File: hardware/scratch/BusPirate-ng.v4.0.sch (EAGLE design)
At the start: 131 parts, among them CON1 CON-USB-F-MICRO-B, IC1 IC_UC_STM32F103RBTXX-LQFP64, IC10 74LVC1G07DBV, IC11 IC_BUFF_SN74LVC1T45DBV, IC12 74LVC1G07DBV, IC13 IC_BUFF_SN74LVC1T45DBV, IC14 74LVC1G07DBV, IC15 IC_BUFF_SN74LVC1T45DBV, IC16 74LVC1G07DBV, IC17 IC_BUFF_SN74LVC1T45DBV, IC2 IC_MEM_23LC1024, IC3 IC_MEM_23LC1024, IC4 IC_74AC573, IC5 IC_BL1551, IC6 IC_BL1551, IC7 74HCT4066PW, IC8 74LVC1G07DBV, IC9 IC_BUFF_SN74LVC1T45DBV, J1 CON_HEADER_1X04, J2 CON_HEADER_1X03-PTH, J3 CON_HEADER_2X02-PTH, J4 CON_HEADER_1X10-RIGHT_ANGLED_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, U1 IC_FPGA_ICE40HX4K, U2 IC_UC_STM32F103ZX, U3 IC_MEM_AT45DB041D

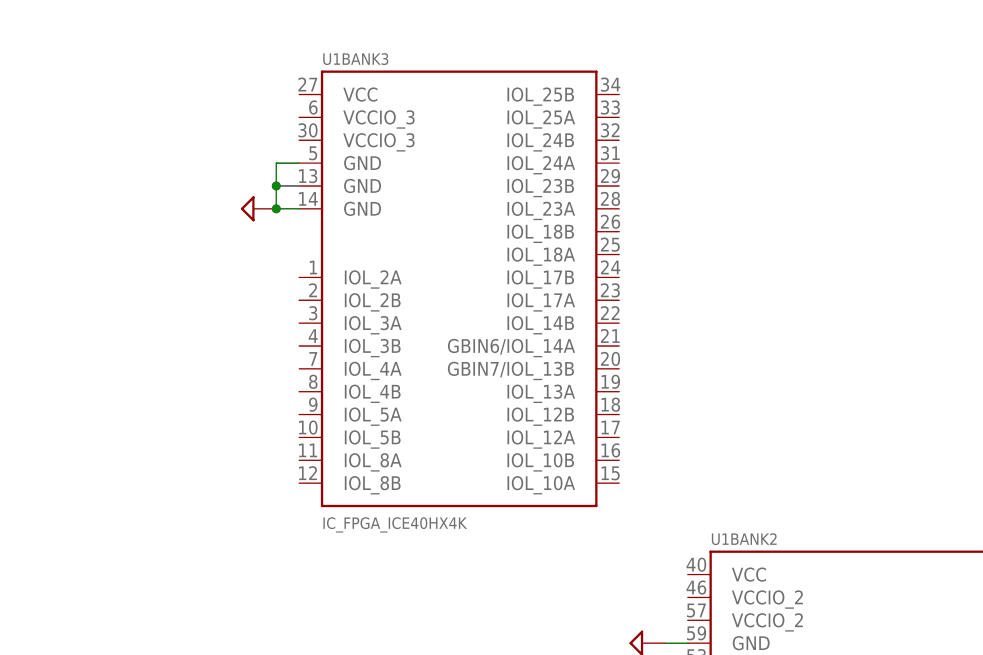
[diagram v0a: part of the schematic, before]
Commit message: connect ARM chip's FSMC address, data and control pins except CS to FPGA
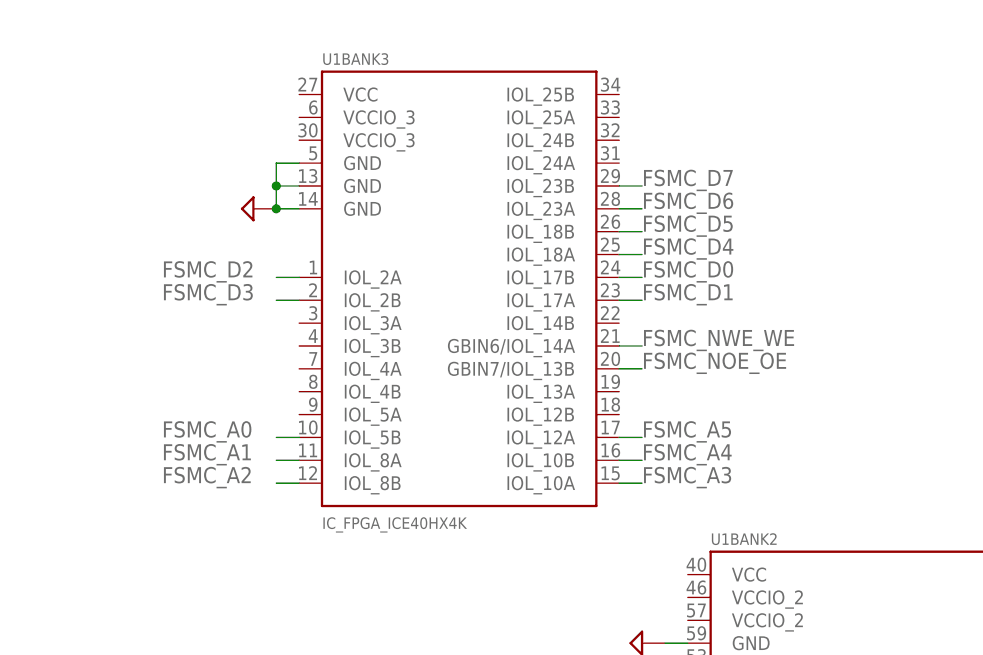
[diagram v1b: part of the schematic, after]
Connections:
- net FSMC_A0: now also U1BANK3.IOL_5B
- net FSMC_A1: now also U1BANK3.IOL_8A
- net FSMC_A2: now also U1BANK3.IOL_8B
- net FSMC_A3: now also U1BANK3.IOL_10A
- net FSMC_A4: now also U1BANK3.IOL_10B
- net FSMC_A5: now also U1BANK3.IOL_12A
- net FSMC_D0: now also U1BANK3.IOL_17B
- net FSMC_D1: now also U1BANK3.IOL_17A
- net FSMC_D2: now also U1BANK3.IOL_2A
- net FSMC_D3: now also U1BANK3.IOL_2B
- net FSMC_D4: now also U1BANK3.IOL_18A
- net FSMC_D5: now also U1BANK3.IOL_18B
- net FSMC_D6: now also U1BANK3.IOL_23A
- net FSMC_D7: now also U1BANK3.IOL_23B
- net FSMC_NOE_OE: now also U1BANK3.GBIN7/IOL_13B
- net FSMC_NWE_WE: now also U1BANK3.GBIN6/IOL_14A
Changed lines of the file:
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@@
 <label x="-241.3" y="426.72" size="1.778" layer="95"/>
+</segment>
+<segment>
+<pinref part="U1" gate="BANK3" pin="IOL_2A"/>
+<wire x1="-38.1" y1="396.24" x2="-40.64" y2="396.24" width="0.1524" layer="91"/>
+<label x="-53.34" y="396.24" size="1.778" layer="95"/>
 </segment>
 </net>
@@
 <label x="-241.3" y="424.18" size="1.778" layer="95"/>
 </segment>
+<segment>
+<pinref part="U1" gate="BANK3" pin="IOL_2B"/>
+<wire x1="-38.1" y1="393.7" x2="-40.64" y2="393.7" width="0.1524" layer="91"/>
+<label x="-53.34" y="393.7" size="1.778" layer="95"/>
+</segment>
 </net>
 <net name="FSMC_NOE_OE" class="0">
@@
 <wire x1="-215.9" y1="416.56" x2="-228.6" y2="416.56" width="0.1524" layer="91"/>
 <label x="-241.3" y="416.56" size="1.778" layer="95"/>
+</segment>
+<segment>
+<pinref part="U1" gate="BANK3" pin="GBIN7/IOL_13B"/>
+<wire x1="-2.54" y1="386.08" x2="0" y2="386.08" width="0.1524" layer="91"/>
+<label x="0" y="386.08" size="1.778" layer="95"/>
 </segment>
 </net>
@@
 <label x="-241.3" y="414.02" size="1.778" layer="95"/>
 </segment>
+<segment>
+<pinref part="U1" gate="BANK3" pin="GBIN6/IOL_14A"/>
+<wire x1="-2.54" y1="388.62" x2="0" y2="388.62" width="0.1524" layer="91"/>
+<label x="0" y="388.62" size="1.778" layer="95"/>
+</segment>
 </net>
 <net name="FSMC_D0" class="0">
@@
 <wire x1="-215.9" y1="391.16" x2="-228.6" y2="391.16" width="0.1524" layer="91"/>
 <label x="-238.76" y="391.16" size="1.778" layer="95"/>
+</segment>
+<segment>
+<pinref part="U1" gate="BANK3" pin="IOL_17B"/>
+<wire x1="-2.54" y1="396.24" x2="0" y2="396.24" width="0.1524" layer="91"/>
+<label x="0" y="396.24" size="1.778" layer="95"/>
 </segment>
 </net>
@@
 <label x="-238.76" y="388.62" size="1.778" layer="95"/>
 </segment>
+<segment>
+<pinref part="U1" gate="BANK3" pin="IOL_17A"/>
+<wire x1="-2.54" y1="393.7" x2="0" y2="393.7" width="0.1524" layer="91"/>
+<label x="0" y="393.7" size="1.778" layer="95"/>
+</segment>
 </net>
 <net name="FSMC_D4" class="0">
@@
 <wire x1="-215.9" y1="365.76" x2="-228.6" y2="365.76" width="0.1524" layer="91"/>
 <label x="-238.76" y="365.76" size="1.778" layer="95"/>
+</segment>
+<segment>
+<pinref part="U1" gate="BANK3" pin="IOL_18A"/>
+<wire x1="-2.54" y1="398.78" x2="0" y2="398.78" width="0.1524" layer="91"/>
+<label x="0" y="398.78" size="1.778" layer="95"/>
 </segment>
 </net>
@@
 <label x="-238.76" y="363.22" size="1.778" layer="95"/>
 </segment>
+<segment>
+<pinref part="U1" gate="BANK3" pin="IOL_18B"/>
+<wire x1="-2.54" y1="401.32" x2="0" y2="401.32" width="0.1524" layer="91"/>
+<label x="0" y="401.32" size="1.778" layer="95"/>
+</segment>
 </net>
 <net name="FSMC_D6" class="0">
@@
 <label x="-238.76" y="360.68" size="1.778" layer="95"/>
 </segment>
+<segment>
+<pinref part="U1" gate="BANK3" pin="IOL_23A"/>
+<wire x1="-2.54" y1="403.86" x2="0" y2="403.86" width="0.1524" layer="91"/>
+<label x="0" y="403.86" size="1.778" layer="95"/>
+</segment>
 </net>
 <net name="FSMC_D7" class="0">
@@
 <wire x1="-215.9" y1="358.14" x2="-228.6" y2="358.14" width="0.1524" layer="91"/>
 <label x="-238.76" y="358.14" size="1.778" layer="95"/>
+</segment>
+<segment>
+<pinref part="U1" gate="BANK3" pin="IOL_23B"/>
+<wire x1="-2.54" y1="406.4" x2="0" y2="406.4" width="0.1524" layer="91"/>
+<label x="0" y="406.4" size="1.778" layer="95"/>
 </segment>
 </net>
@@
 <label x="-99.06" y="383.54" size="1.778" layer="95"/>
 </segment>
+<segment>
+<pinref part="U1" gate="BANK3" pin="IOL_5B"/>
+<wire x1="-38.1" y1="378.46" x2="-40.64" y2="378.46" width="0.1524" layer="91"/>
+<label x="-53.34" y="378.46" size="1.778" layer="95"/>
+</segment>
 </net>
 <net name="FSMC_A1" class="0">
@@
 <wire x1="-109.22" y1="381" x2="-99.06" y2="381" width="0.1524" layer="91"/>
 <label x="-99.06" y="381" size="1.778" layer="95"/>
+</segment>
+<segment>
+<pinref part="U1" gate="BANK3" pin="IOL_8A"/>
+<wire x1="-38.1" y1="375.92" x2="-40.64" y2="375.92" width="0.1524" layer="91"/>
+<label x="-53.34" y="375.92" size="1.778" layer="95"/>
 </segment>
 </net>
@@
 <label x="-99.06" y="378.46" size="1.778" layer="95"/>
 </segment>
+<segment>
+<pinref part="U1" gate="BANK3" pin="IOL_8B"/>
+<wire x1="-38.1" y1="373.38" x2="-40.64" y2="373.38" width="0.1524" layer="91"/>
+<label x="-53.34" y="373.38" size="1.778" layer="95"/>
+</segment>
 </net>
 <net name="FSMC_A3" class="0">
@@
 <wire x1="-109.22" y1="375.92" x2="-99.06" y2="375.92" width="0.1524" layer="91"/>
 <label x="-99.06" y="375.92" size="1.778" layer="95"/>
+</segment>
+<segment>
+<pinref part="U1" gate="BANK3" pin="IOL_10A"/>
+<wire x1="-2.54" y1="373.38" x2="0" y2="373.38" width="0.1524" layer="91"/>
+<label x="0" y="373.38" size="1.778" layer="95"/>
 </segment>
 </net>
@@
 <label x="-99.06" y="373.38" size="1.778" layer="95"/>
 </segment>
+<segment>
+<pinref part="U1" gate="BANK3" pin="IOL_10B"/>
+<wire x1="-2.54" y1="375.92" x2="0" y2="375.92" width="0.1524" layer="91"/>
+<label x="0" y="375.92" size="1.778" layer="95"/>
+</segment>
 </net>
 <net name="FSMC_A5" class="0">
@@
 <label x="-99.06" y="370.84" size="1.778" layer="95"/>
 </segment>
+<segment>
+<pinref part="U1" gate="BANK3" pin="IOL_12A"/>
+<wire x1="-2.54" y1="378.46" x2="0" y2="378.46" width="0.1524" layer="91"/>
+<label x="0" y="378.46" size="1.778" layer="95"/>
+</segment>
 </net>

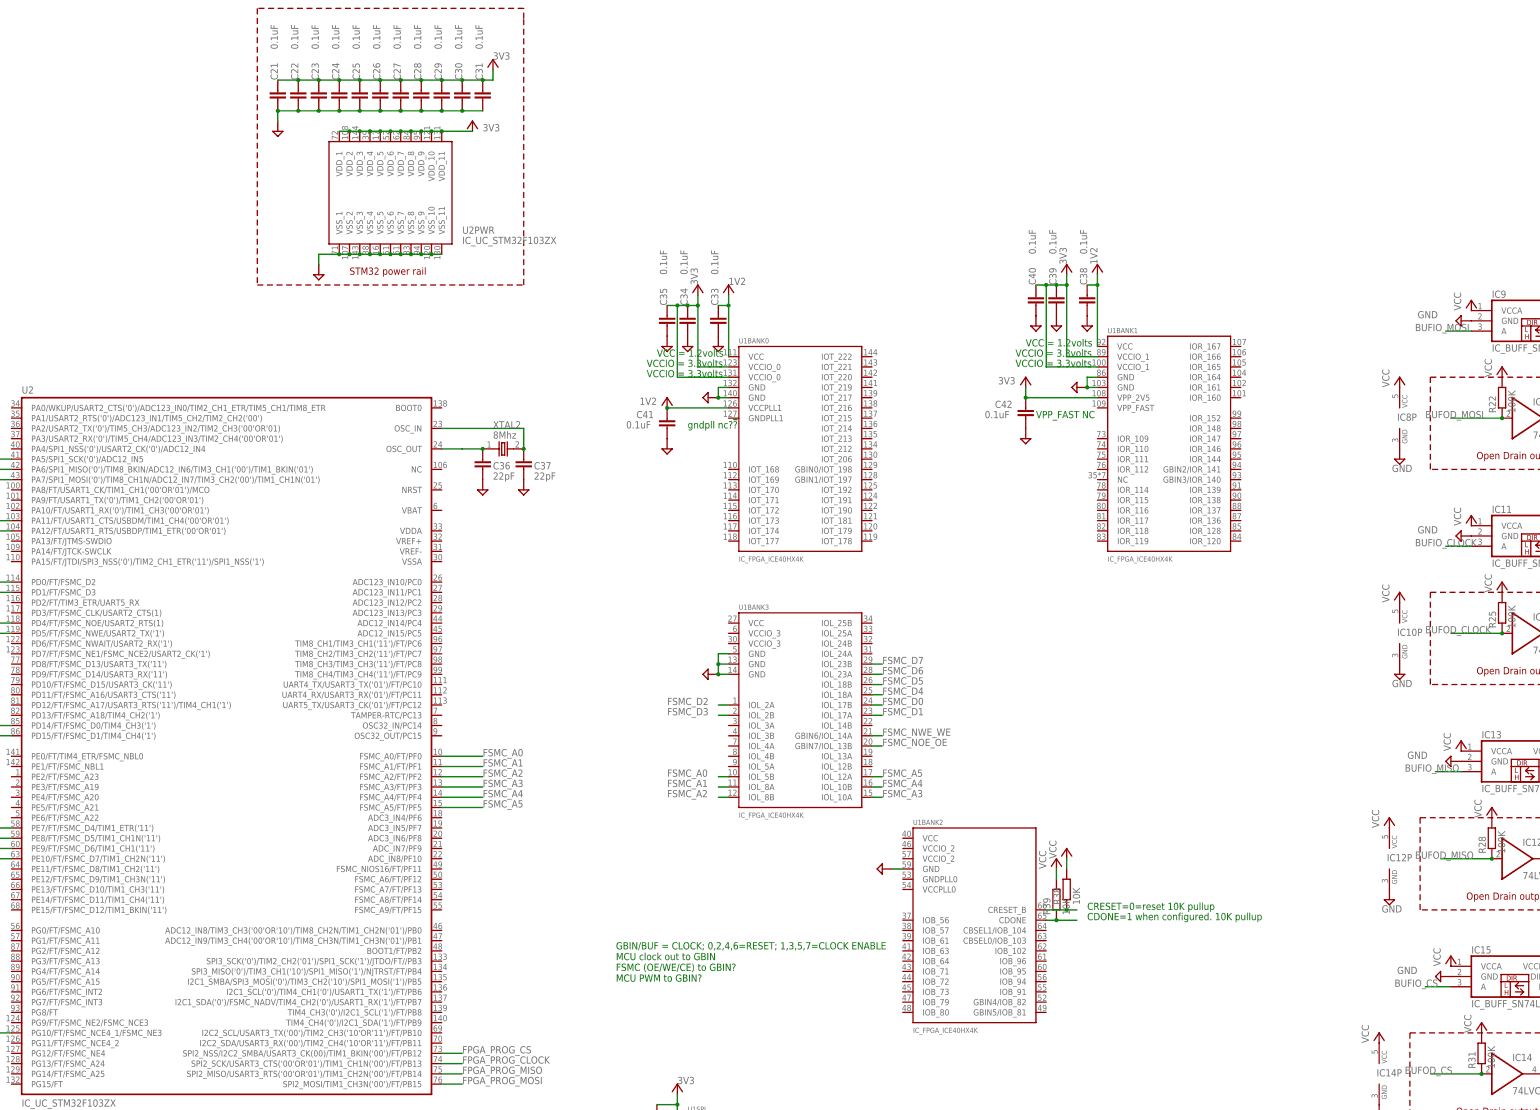
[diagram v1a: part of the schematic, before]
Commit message: connect power 1.2V and 3.3V for bank 2 and 3 of FPGA
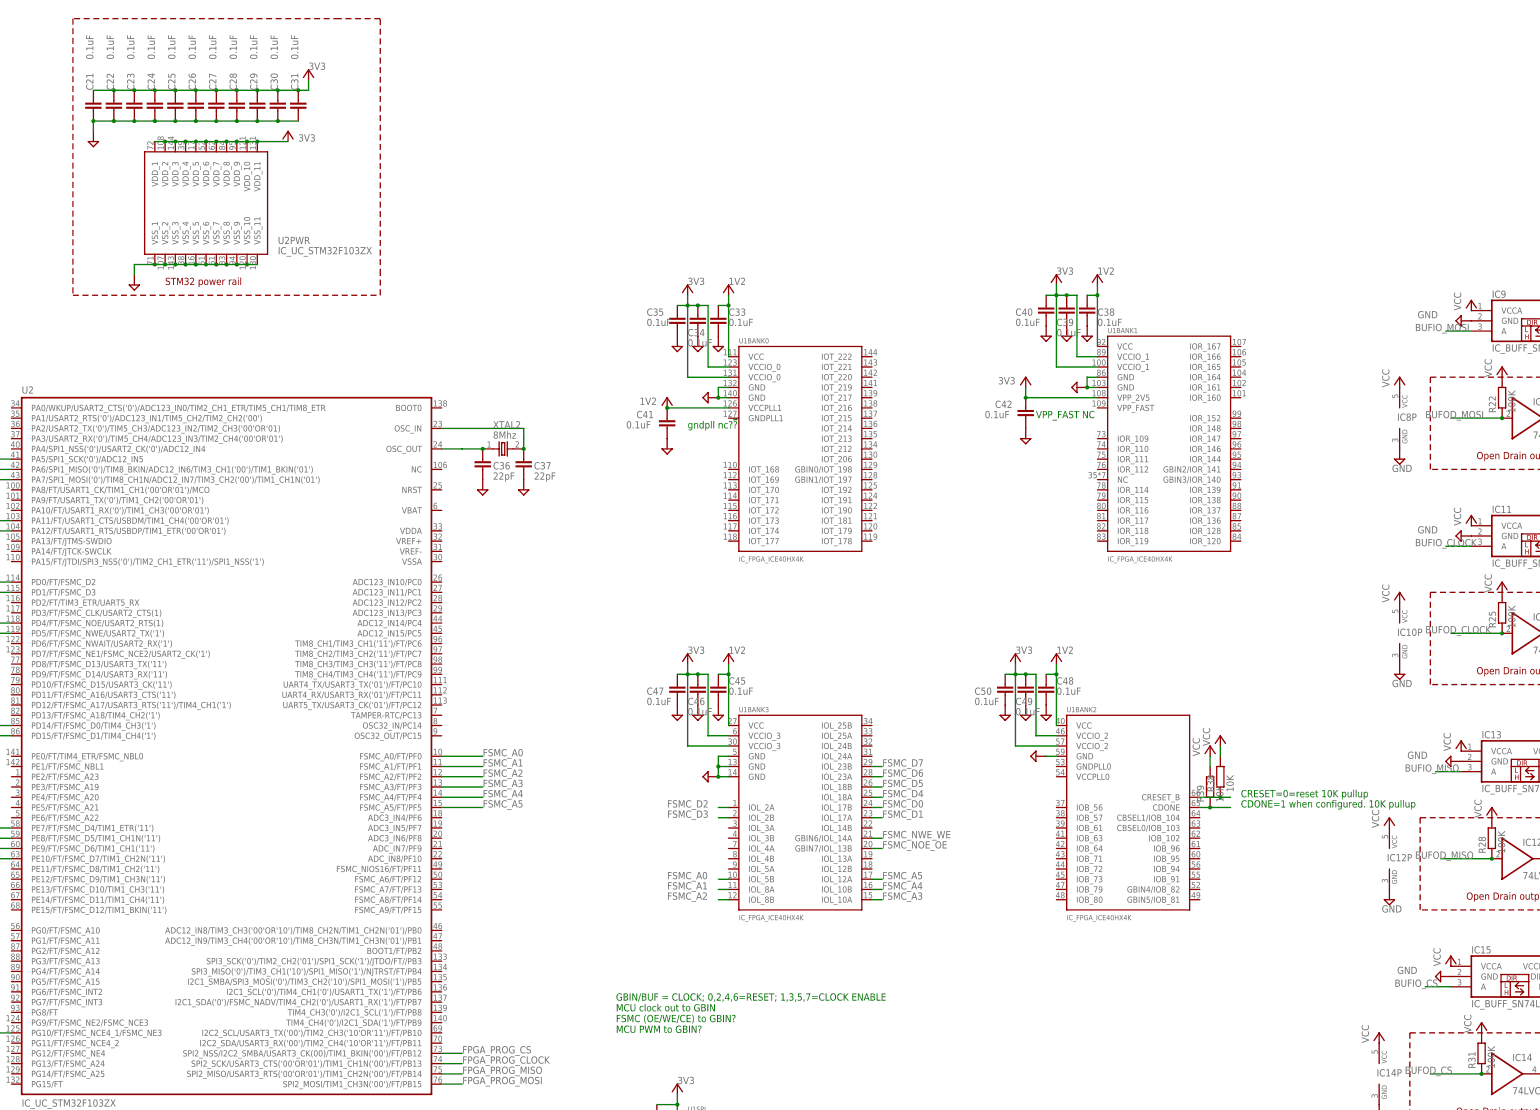
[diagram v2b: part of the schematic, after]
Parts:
- added C45, C46, C47, C48, C49, C50: 0.1uF, rcl:C-EUC0603
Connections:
- net 1V2: now also C45.2, C48.2, U1BANK2.VCC@0, U1BANK3.VCC@0
- net 3V3: now also C46.2, C47.2, C49.2, C50.2, U1BANK2.VCCIO_2@0, U1BANK2.VCCIO_2@1, U1BANK3.VCCIO_3@0, U1BANK3.VCCIO_3@1
- net GND: now also C45.1, C46.1, C47.1, C48.1, C49.1, C50.1
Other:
- note removed: "VCC = 1.2volts"
- note removed: "VCCIO = 3.3volts"
- moved on the sheet: C21, C22, C23, C24, C25, C26, C27, C28, C29, C30, C31, C34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

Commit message: wired -BOOT0 and BOOT1 to corresponding switches -NRST to reset switch -VBAT with 0.1uF cap to 3V3 -VDDA with 0.1uF and 1uF cap to 3V3 -VSSA to GND -PC0 - PC4 to ADC2 - AD6 -control pins pull ups VEXTPU, IO_OE, LD1 and USBLED -PB0 to AUX0 -PB1 to ADC1 -control pins PB3, PB4, PB5 and PB6 to SRAM_CS, V50PU, V33PU and VREGEN respectively -UART TX and UART RX to PA9 and PA10 -programming pins SWDIO and SWCLK to PA13 and PA14 -USB detect to PA15
added connection but not wired yet to FPGA
-FSMC_D8 to D15
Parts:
- added C51, C52, C54: 0.1uF, rcl:C-EUC0603
- added C53: 1uF, rcl:CPOL-EUSMCA
- added R40: 10K, dp_devices:RESISTOR-0603
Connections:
- new net FSMC_D10: U2U.PE13/FT/FSMC_D10/TIM1_CH3('11')
- new net FSMC_D11: U2U.PE14/FT/FSMC_D11/TIM1_CH4('11')
- new net FSMC_D12: U2U.PE15/FT/FSMC_D12/TIM1_BKIN('11')
- new net FSMC_D13: U2U.PD8/FT/FSMC_D13/USART3_TX('11')
- new net FSMC_D14: U2U.PD9/FT/FSMC_D14/USART3_RX('11')
- new net FSMC_D15: U2U.PD10/FT/FSMC_D15/USART3_CK('11')
- new net FSMC_D8: U2U.PE11/FT/FSMC_D8/TIM1_CH2('11')
- new net FSMC_D9: U2U.PE12/FT/FSMC_D9/TIM1_CH3N('11')
- net 3V3: now also C52.2, C53.+, C54.2, U2U.VBAT, U2U.VDDA
- net ADC1: now also U2U.ADC12_IN9/TIM3_CH4('00'OR'10')/TIM8_CH3N/TIM1_CH3N('01')/PB1
- net ADC2: now also U2U.ADC123_IN13/PC3
- net ADC3: now also U2U.ADC123_IN11/PC1
- net ADC4: now also U2U.ADC123_IN12/PC2
- net ADC5: now also U2U.ADC123_IN10/PC0
- net ADC6: now also U2U.ADC12_IN14/PC4
- net AUX0: now also U2U.ADC12_IN8/TIM3_CH3('00'OR'10')/TIM8_CH2N/TIM1_CH2N('01')/PB0
- net BOOT0: now also U2U.BOOT0
- net BOOT1: now also U2U.BOOT1/FT/PB2
- net GND: now also C51.1, C52.1, C53.-, C54.1, R40.2, U2U.VSSA
- net IO_OE: now also U2U.TIM8_CH2/TIM3_CH2('11')/FT/PC7
- net LD1: now also U2U.TIM8_CH3/TIM3_CH3('11')/FT/PC8
- net RST: now also C51.2, U2U.NRST
- net SRAM_CS: now also U2U.SPI3_SCK('0')/TIM2_CH2('01')/SPI1_SCK('1')/JTDO/FT//PB3
- net SWCLK: now also U2U.PA14/FT/JTCK-SWCLK
- net SWDIO: now also U2U.PA13/FT/JTMS-SWDIO
- net UART_RX: now also U2U.PA10/FT/USART1_RX('0')/TIM1_CH3('00'OR'01')
- net UART_TX: now also U2U.PA9/FT/USART1_TX('0')/TIM1_CH2('00'OR'01')
- net USBLED: now also U2U.TIM8_CH4/TIM3_CH4('11')/FT/PC9
- net USB_DET: now also U2U.PA15/FT/JTDI/SPI3_NSS('0')/TIM2_CH1_ETR('11')/SPI1_NSS('1')
- net V33PU: now also U2U.I2C1_SMBA/SPI3_MOSI('0')/TIM3_CH2('10')/SPI1_MOSI('1')/PB5
- net V50PU: now also U2U.SPI3_MISO('0')/TIM3_CH1('10')/SPI1_MISO('1')/NJTRST/FT/PB4
- net VEXTPU: now also U2U.TIM8_CH1/TIM3_CH1('11')/FT/PC6
- net VREGEN: now also R40.1, U2U.I2C1_SCL('0')/TIM4_CH1('0')/USART1_TX('1')/FT/PB6
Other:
- note added: "wire SRAM_CLK to FPGA global pin clock"
- moved on the sheet: C36, C37, J3, R18, R3, R4, SW2, XTAL2
